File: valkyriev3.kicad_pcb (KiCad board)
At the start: 4 copper layers, 70 x 100 mm, 125 parts, among them J1 USB_C_Receptacle_USB2.0_16P, J10 Conn_01x03, J11 Conn_01x03, J2 DE9_Pins_MountingHoles, J3 SMA_180C, J4 SMA_180C, J5 Conn_01x02_Socket, J6 Conn_01x02_Socket, J7 Conn_01x02_Socket, J8 Conn_01x03, J9 Conn_01x05, Q1 BC817, Q2 BC817, Q3 BC817, Q4 BC817, Q5 BC817, Q6 DMG3420U, Q7 DMP2305U, Q8 DMG3420U, SW1 SW_SPST, SW2 SW_SPST, U1 W25Q128JVS, U10 LPS22HB, U2 ESP32-S3-MINI-1U, U3 MAX3232, U4 AMS1117-3.3, U5 TPS562202, U9 MS5607-02BA

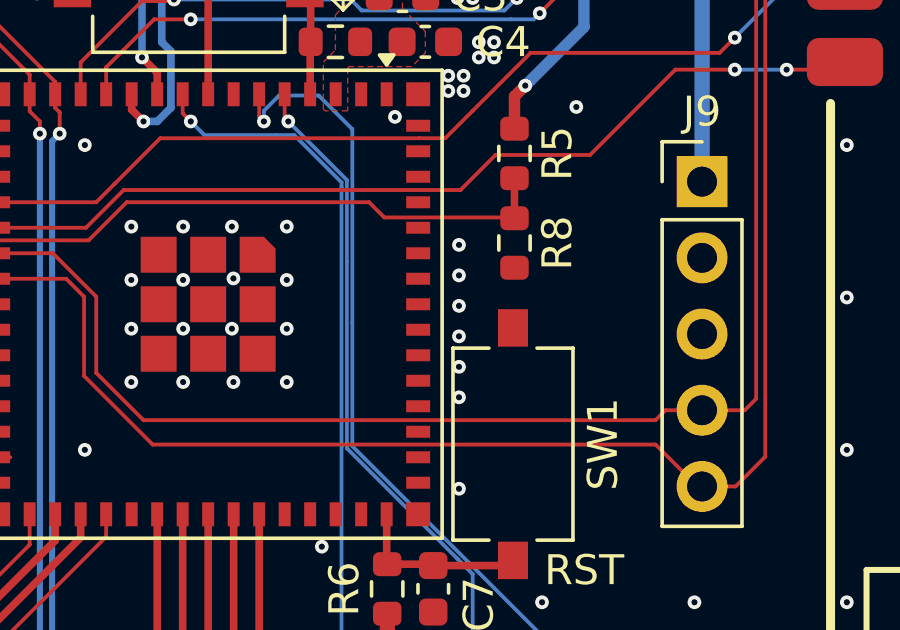
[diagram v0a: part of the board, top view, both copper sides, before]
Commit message: connected missing grounds
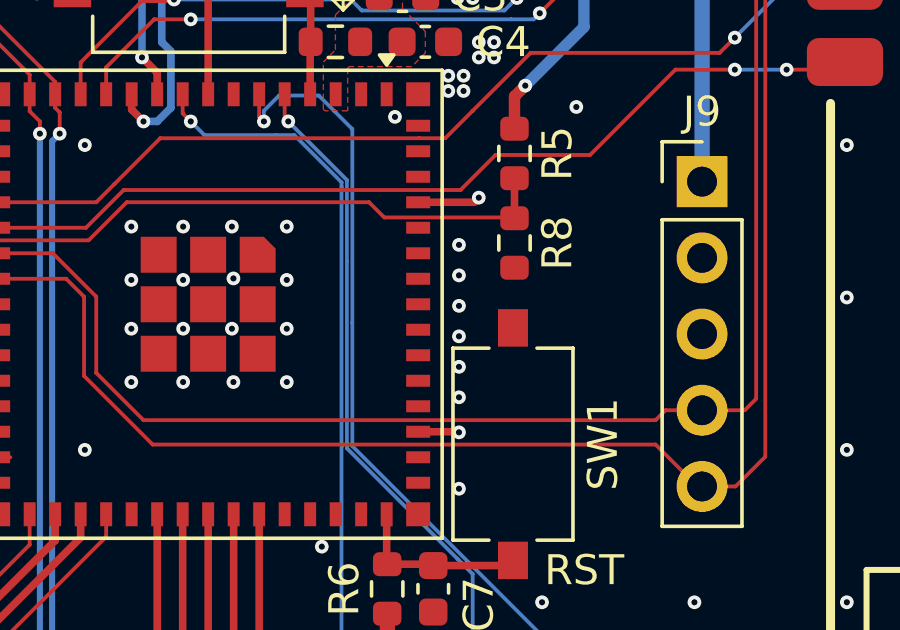
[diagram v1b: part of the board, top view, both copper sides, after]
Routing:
- net GND: track 21.4 -> 24.9 mm, vias 363 -> 365
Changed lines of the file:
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@@
+	)
+	(segment
+		(start 128.4212 91.4412)
+		(end 128.5748 91.2876)
+		(width 0.254)
+		(layer "F.Cu")
+		(net 2)
 	)
 	(segment
 		(start 140.97 123.7966)
 		(end 140.9899 123.7767)
+		(width 0.254)
+		(layer "F.Cu")
+		(net 2)
+	)
+	(segment
+		(start 126.554 91.4412)
+		(end 128.4212 91.4412)
 		(width 0.254)
 		(layer "F.Cu")
@@
 	)
 	(segment
+		(start 126.554 99.0912)
+		(end 127.8948 99.0912)
+		(width 0.254)
+		(layer "F.Cu")
+		(net 2)
+	)
+	(segment
+		(start 127.8948 99.0912)
+		(end 127.9144 99.1108)
+		(width 0.254)
+		(layer "F.Cu")
+		(net 2)
+	)
+	(segment
 		(start 105.4334 91.0062)
 		(end 104.288 91.0062)
@@
 	)
 	(via
+		(at 127.9144 99.1108)
+		(size 0.4572)
+		(drill 0.2032)
+		(layers "F.Cu" "B.Cu")
+		(free yes)
+		(net 2)
+	)
+	(via
 		(at 120.523 53.975)
 		(size 0.4572)
@@
 		(size 0.4572)
 		(drill 0.2032)
+		(layers "F.Cu" "B.Cu")
+		(free yes)
+		(net 2)
+	)
+	(via
+		(at 128.5748 91.2876)
+		(size 0.4572)
+		(drill 0.2032)

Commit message: added my name as reviewer to pcb
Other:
- board text added: "GUNALTAY ROCKET TEAM Valkyrie V3 Flight Computer Drawn By: S. Kömürcüoğlu Reviewed By: Ö.T. Önsoy VIN: 7-15V DC"
- board text removed: "GUNALTAY ROCKET TEAM Valkyrie V3 Flight Computer Drawn By: Süalp K. VIN: 7-15V DC"
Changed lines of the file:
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@@
 			(psa4output no)
 			(plot_black_and_white yes)
+			(plotinvisibletext no)
 			(sketchpadsonfab no)
 			(plotpadnumbers no)
@@
 		)
 	)
-	(gr_text "GUNALTAY ROCKET TEAM\nValkyrie V3\nFlight Computer\n\nDrawn By: Süalp K.\nVIN: 7-15V DC"
-		(at 152.8064 89.662 0)
+	(gr_text "GUNALTAY ROCKET TEAM\nValkyrie V3\nFlight Computer\n\nDrawn By: S. Kömürcüoğlu\nReviewed By: Ö.T. Önsoy\nVIN: 7-15V DC"
+		(at 152.8064 90.92 0)
 		(layer "B.SilkS")
 		(effects

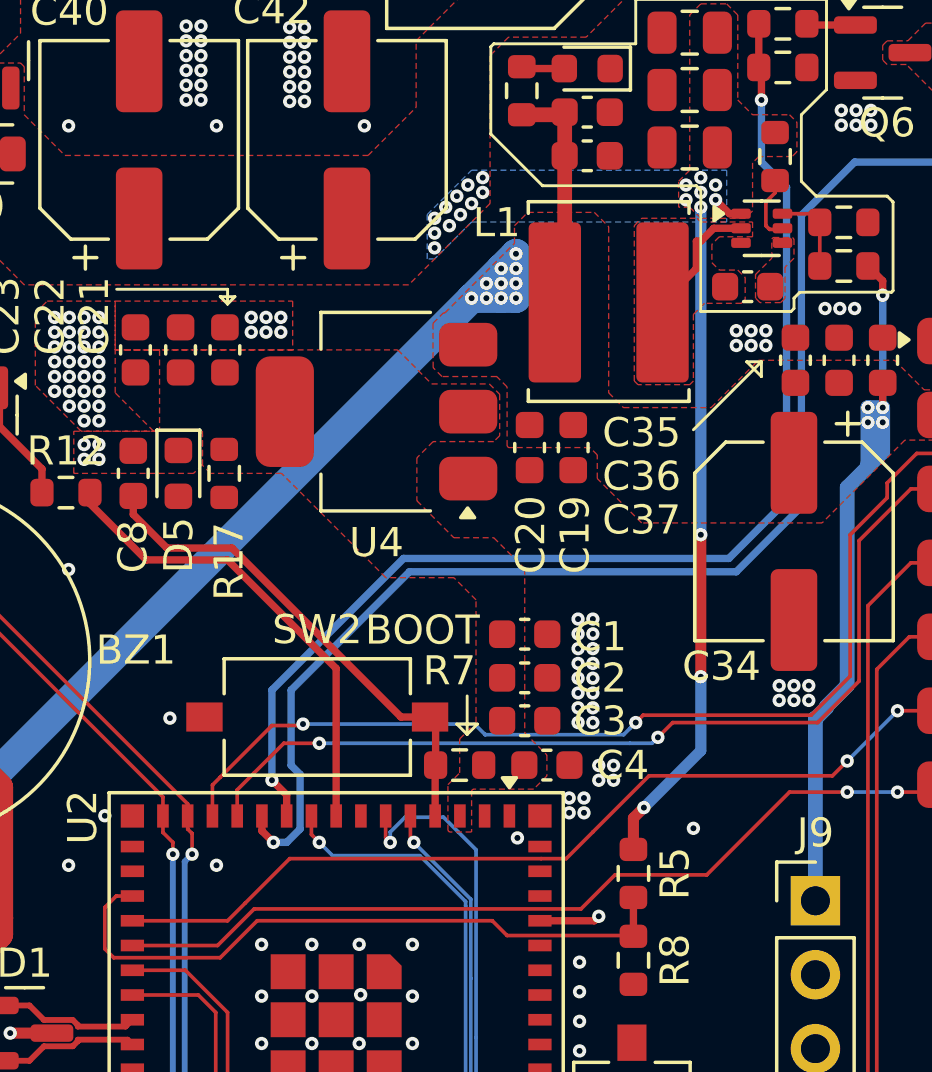
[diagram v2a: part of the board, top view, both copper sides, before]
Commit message: fixed unconnected grounds
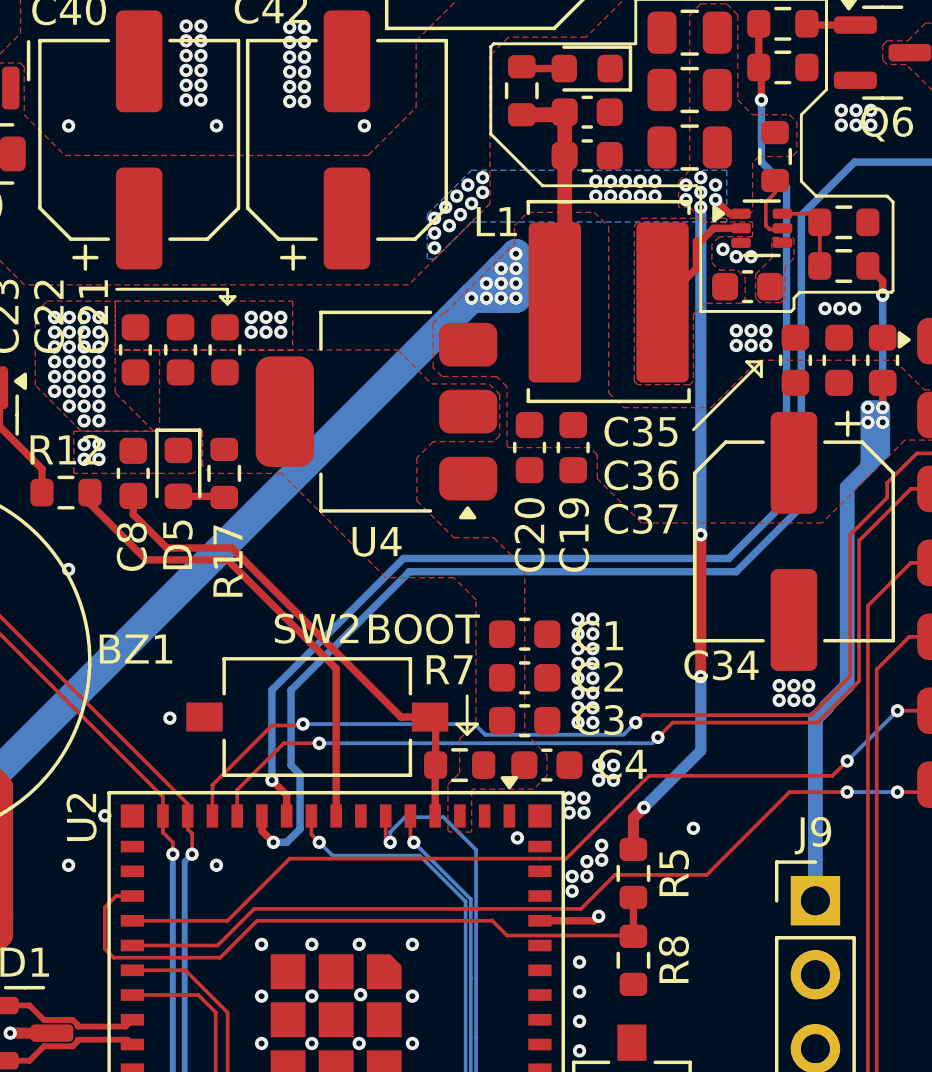
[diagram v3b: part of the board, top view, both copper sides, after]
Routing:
- net /Power/3V3_LED: track 0.00 -> 1.59 mm
- net GND: vias 365 -> 384
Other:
- board text added: "GUNALTAY ROCKET TEAM Valkyrie V3 Flight Computer Drawn By: S. KÖMÜRCÜOĞLU Reviewed By: Ö.T. ÖNSOY VIN: 7-15V DC"
- board text removed: "GUNALTAY ROCKET TEAM Valkyrie V3 Flight Computer Drawn By: S. Kömürcüoğlu Reviewed By: Ö.T. Önsoy VIN: 7-15V DC"
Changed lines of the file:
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@@
 			(psa4output no)
 			(plot_black_and_white yes)
-			(plotinvisibletext no)
 			(sketchpadsonfab no)
 			(plotpadnumbers no)
@@
 		)
 	)
-	(gr_text "GUNALTAY ROCKET TEAM\nValkyrie V3\nFlight Computer\n\nDrawn By: S. Kömürcüoğlu\nReviewed By: Ö.T. Önsoy\nVIN: 7-15V DC"
-		(at 152.8064 90.92 0)
+	(gr_text "GUNALTAY ROCKET TEAM\nValkyrie V3\nFlight Computer\n\nDrawn By: S. KÖMÜRCÜOĞLU\nReviewed By: Ö.T. ÖNSOY\n\nVIN: 7-15V DC"
+		(at 152.8064 91.694 0)
 		(layer "B.SilkS")
 		(effects
@@
 	)
 	(via
+		(at 128.1684 89.408)
+		(size 0.4572)
+		(drill 0.2032)
+		(layers "F.Cu" "B.Cu")
+		(free yes)
+		(net 2)
+	)
+	(via
 		(at 106.7308 99.7712)
 		(size 0.4572)
@@
 	)
 	(via
+		(at 132.842 68.3768)
+		(size 0.4572)
+		(drill 0.2032)
+		(layers "F.Cu" "B.Cu")
+		(free yes)
+		(net 2)
+	)
+	(via
 		(at 103.2764 122.428)
 		(size 0.4572)
@@
 	)
 	(via
+		(at 130.5052 66.548)
+		(size 0.4572)
+		(drill 0.2032)
+		(layers "F.Cu" "B.Cu")
+		(free yes)
+		(net 2)
+	)
+	(via
 		(at 161.163 89.535)
 		(size 0.4572)
@@
 	)
 	(via
+		(at 128.9812 66.04)
+		(size 0.4572)
+		(drill 0.2032)
+		(layers "F.Cu" "B.Cu")
+		(free yes)
+		(net 2)
+	)
+	(via
 		(at 128.3716 84.1248)
 		(size 0.4572)
@@
 	)
 	(via
+		(at 128.6764 89.3572)
+		(size 0.4572)
+		(drill 0.2032)
+		(layers "F.Cu" "B.Cu")
+		(free yes)
+		(net 2)
+	)
+	(via
 		(at 118.4656 61.2648)
 		(size 0.4572)
@@
 	)
 	(via
+		(at 130.5052 66.04)
+		(size 0.4572)
+		(drill 0.2032)
+		(layers "F.Cu" "B.Cu")
+		(free yes)
+		(net 2)
+	)
+	(via
 		(at 136.3472 70.4088)
 		(size 0.4572)
@@
 	)
 	(via
+		(at 133.8072 68.6308)
+		(size 0.4572)
+		(drill 0.2032)
+		(layers "F.Cu" "B.Cu")
+		(free yes)
+		(net 2)
+	)
+	(via
 		(at 120.7516 55.626)
 		(size 0.4572)
@@
 	)
 	(via
+		(at 129.4892 66.04)
+		(size 0.4572)
+		(drill 0.2032)
+		(layers "F.Cu" "B.Cu")
+		(free yes)
+		(net 2)
+	)
+	(via
 		(at 103.4288 68.072)
 		(size 0.4572)
@@
 	)
 	(via
+		(at 128.4732 66.04)
+		(size 0.4572)
+		(drill 0.2032)
+		(layers "F.Cu" "B.Cu")
+		(free yes)
+		(net 2)
+	)
+	(via
 		(at 128.0668 87.7316)
 		(size 0.4572)
@@
 	)
 	(via
+		(at 129.9972 66.04)
+		(size 0.4572)
+		(drill 0.2032)
+		(layers "F.Cu" "B.Cu")
+		(free yes)
+		(net 2)
+	)
+	(via
 		(at 126.025549 138)
 		(size 0.458)
@@
 	)
 	(via
+		(at 128.9812 66.548)
+		(size 0.4572)
+		(drill 0.2032)
+		(layers "F.Cu" "B.Cu")
+		(free yes)
+		(net 2)
+	)
+	(via
 		(at 122.174 94.0308)
 		(size 0.4572)
@@
 	)
 	(via
+		(at 133.2992 68.6308)
+		(size 0.4572)
+		(drill 0.2032)
+		(layers "F.Cu" "B.Cu")
+		(free yes)
+		(net 2)
+	)
+	(via
 		(at 113.8428 84.4804)
 		(size 0.4572)
@@
 	)
 	(via
+		(at 128.4732 66.548)
+		(size 0.4572)
+		(drill 0.2032)
+		(layers "F.Cu" "B.Cu")
+		(free yes)
+		(net 2)
+	)
+	(via
 		(at 115.1636 123.0376)
 		(size 0.4572)
@@
 	)
 	(via
+		(at 127.6604 89.916)
+		(size 0.4572)
+		(drill 0.2032)
+		(layers "F.Cu" "B.Cu")
+		(free yes)
+		(net 2)
+	)
+	(via
 		(at 156.083 144.907)
 		(size 0.4572)
@@
 	)
 	(via
+		(at 129.9972 66.548)
+		(size 0.4572)
+		(drill 0.2032)
+		(layers "F.Cu" "B.Cu")
+		(free yes)
+		(net 2)
+	)
+	(via
 		(at 156.083 79.375)
 		(size 0.4572)
@@
 	)
 	(via
+		(at 127.6604 90.424)
+		(size 0.4572)
+		(drill 0.2032)
+		(layers "F.Cu" "B.Cu")
+		(free yes)
+		(net 2)
+	)
+	(via
 		(at 110.363 64.135)
 		(size 0.4572)
@@
 	)
 	(via
+		(at 128.1684 89.916)
+		(size 0.4572)
+		(drill 0.2032)
+		(layers "F.Cu" "B.Cu")
+		(free yes)
+		(net 2)
+	)
+	(via
 		(at 156.083 74.295)
 		(size 0.4572)
@@
 	)
 	(via
+		(at 128.6764 88.8492)
+		(size 0.4572)
+		(drill 0.2032)
+		(layers "F.Cu" "B.Cu")
+		(free yes)
+		(net 2)
+	)
+	(via
 		(at 114.9096 62.23)
 		(size 0.4572)
@@
 	)
 	(via
+		(at 129.4892 66.548)
+		(size 0.4572)
+		(drill 0.2032)
+		(layers "F.Cu" "B.Cu")
+		(free yes)
+		(net 2)
+	)
+	(via
 		(at 142.494 72.0852)
 		(size 0.4572)
@@
 	)
 	(segment
+		(start 115.6707 76.8599)
+		(end 115.7082 76.8974)
+		(width 0.254)
+		(layer "F.Cu")
+		(net 27)
+	)
+	(segment
+		(start 114.1334 76.8599)
+		(end 115.6707 76.8599)
+		(width 0.254)
+		(layer "F.Cu")
+		(net 27)
+	)
+	(segment

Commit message: added esat's image
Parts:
- added G***: LOGO, LOGO, B.Cu at (117.0, 80.6)

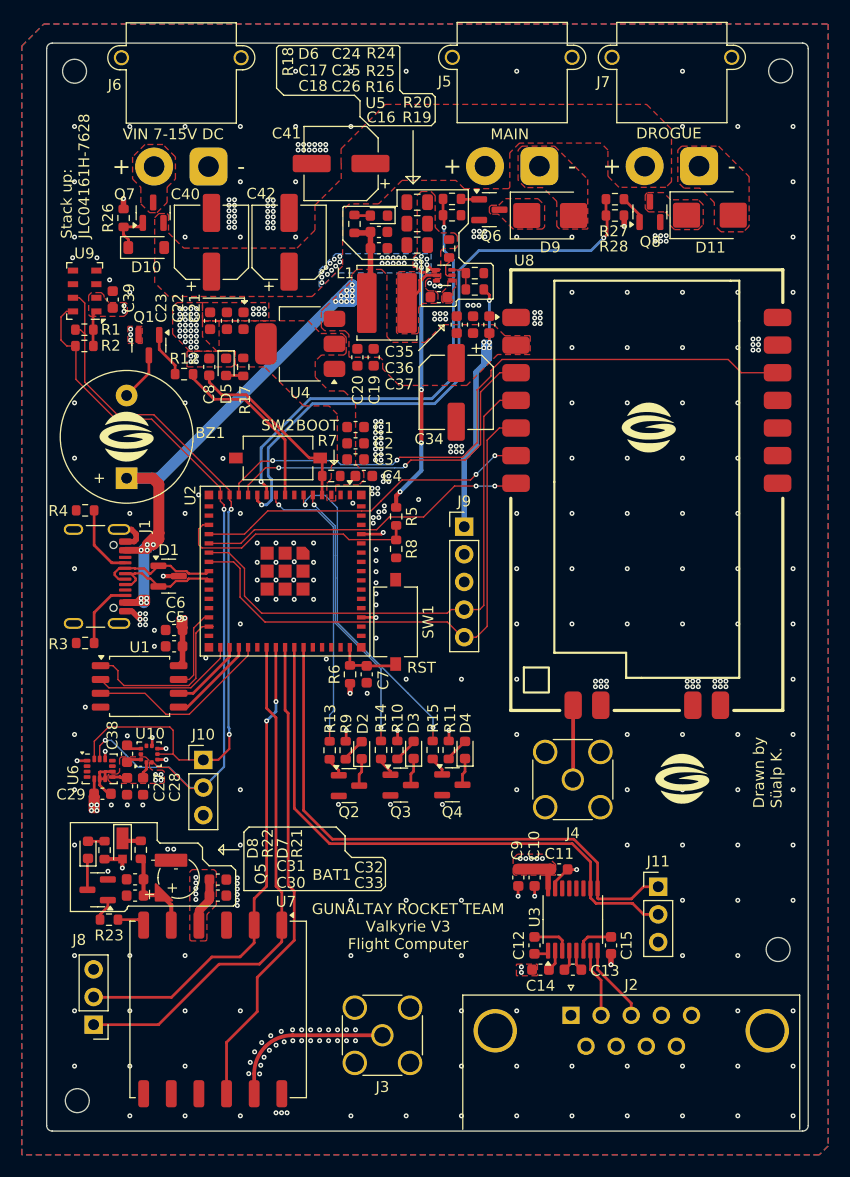
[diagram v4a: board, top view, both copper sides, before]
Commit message: added labels to headers and leds, configured severities of DRC checks
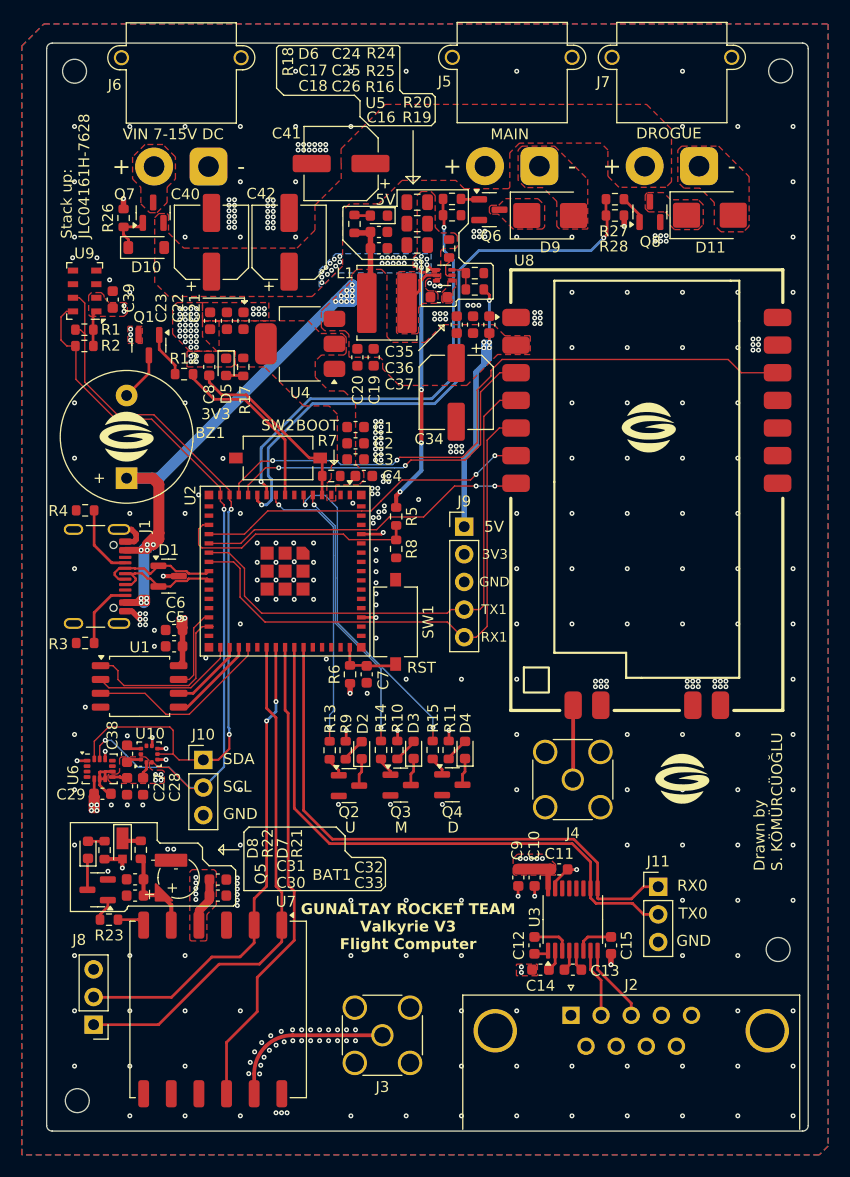
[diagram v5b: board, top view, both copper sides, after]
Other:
- board text added: "3V3"
- board text added: "5V"
- board text added: "D"
- board text added: "Drawn by S. KÖMÜRCÜOĞLU"
- board text added: "GND"
- board text added: "M"
- board text added: "RX0"
- board text added: "RX1"
- board text added: "RX2"
- board text added: "SCL"
- board text added: "SDA"
- board text added: "TX0"
- board text added: "TX1"
- board text added: "TX2"
- board text added: "U"
- board text removed: "Drawn by Süalp K."

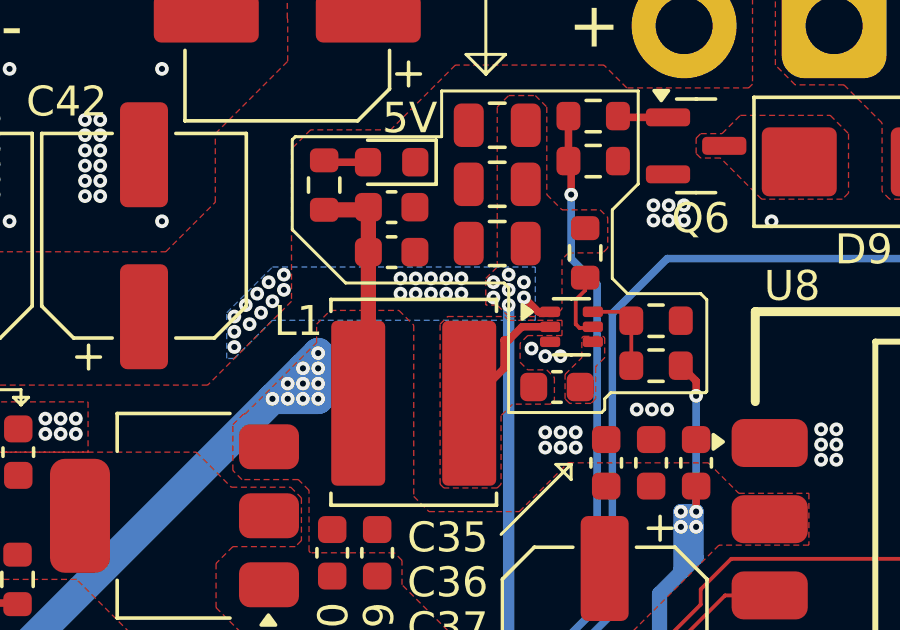
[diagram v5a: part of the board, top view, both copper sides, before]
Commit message: widened VIN track going to 5V SMPS
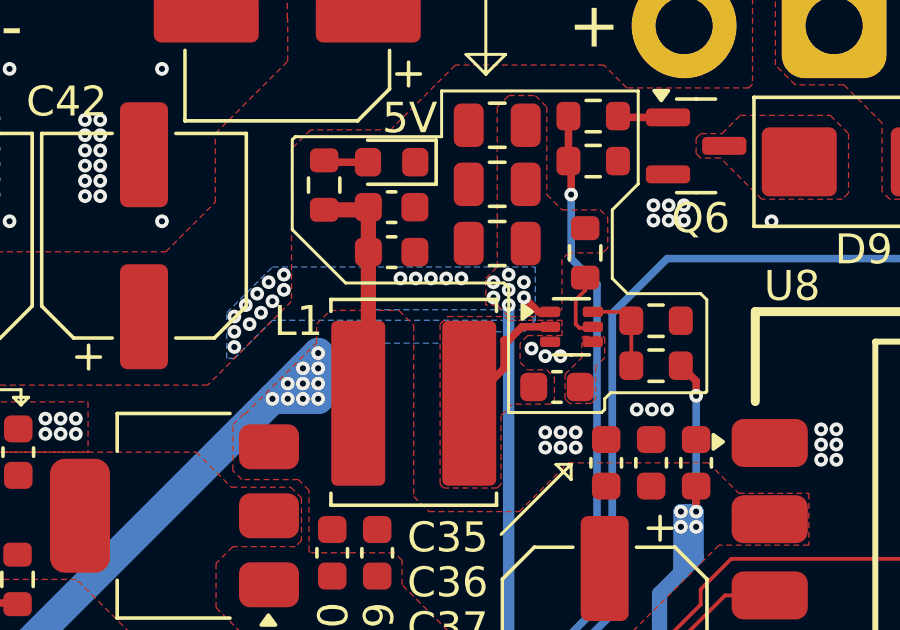
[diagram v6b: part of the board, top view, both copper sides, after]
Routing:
- net GND: vias 384 -> 379
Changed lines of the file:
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@@
 	)
 	(via
-		(at 130.5052 66.548)
-		(size 0.4572)
-		(drill 0.2032)
-		(layers "F.Cu" "B.Cu")
-		(free yes)
-		(net 2)
-	)
-	(via
 		(at 161.163 89.535)
 		(size 0.4572)
@@
 	)
 	(via
-		(at 128.9812 66.548)
-		(size 0.4572)
-		(drill 0.2032)
-		(layers "F.Cu" "B.Cu")
-		(free yes)
-		(net 2)
-	)
-	(via
 		(at 122.174 94.0308)
 		(size 0.4572)
@@
 	)
 	(via
-		(at 128.4732 66.548)
-		(size 0.4572)
-		(drill 0.2032)
-		(layers "F.Cu" "B.Cu")
-		(free yes)
-		(net 2)
-	)
-	(via
 		(at 115.1636 123.0376)
 		(size 0.4572)
@@
 	)
 	(via
-		(at 129.9972 66.548)
-		(size 0.4572)
-		(drill 0.2032)
-		(layers "F.Cu" "B.Cu")
-		(free yes)
-		(net 2)
-	)
-	(via
 		(at 156.083 79.375)
 		(size 0.4572)
@@
 	)
 	(via
-		(at 129.4892 66.548)
-		(size 0.4572)
-		(drill 0.2032)
-		(layers "F.Cu" "B.Cu")
-		(free yes)
-		(net 2)
-	)
-	(via
 		(at 142.494 72.0852)
 		(size 0.4572)
@@
 			)
 		)
+	)
+	(zone
+		(net 18)
+		(net_name "VIN")
+		(layer "B.Cu")
+		(hatch edge 0.5)
+		(priority 12)
+		(connect_pads
+			(clearance 0.3048)
+		)
+		(min_thickness 0.25)
+		(filled_areas_thickness no)
+		(fill yes
+			(thermal_gap 0.5)
+			(thermal_bridge_width 0.5)
+		)
+		(polygon
+			(pts
+				(xy 127.2794 67.0814) (xy 127.2794 67.5386) (xy 127.9398 68.199) (xy 130.937 68.199) (xy 131.318 67.818)
+				(xy 132.588 67.818) (xy 132.969 67.437) (xy 132.6134 67.0814)
+			)
+		)
